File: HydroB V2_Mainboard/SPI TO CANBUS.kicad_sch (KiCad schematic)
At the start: 14 parts, among them J4 Conn_01x02_Pin, U3 MCP2515-xSO, U4 SN65HVD230, Y1 8Mhz

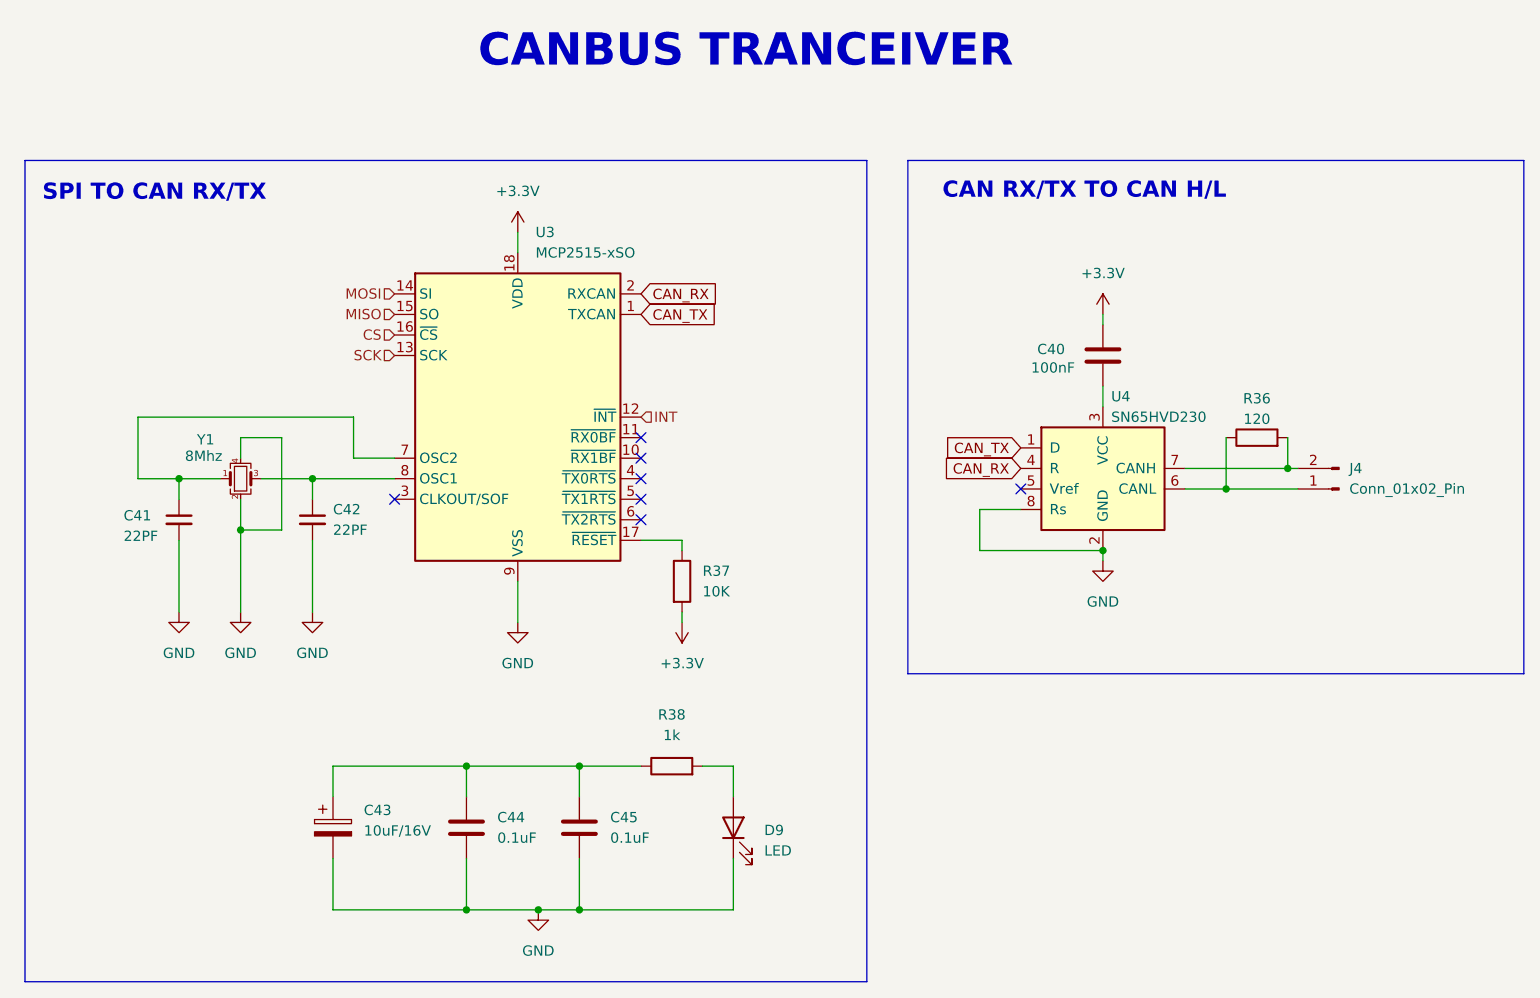
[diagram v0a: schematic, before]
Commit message: Update LCD schematic
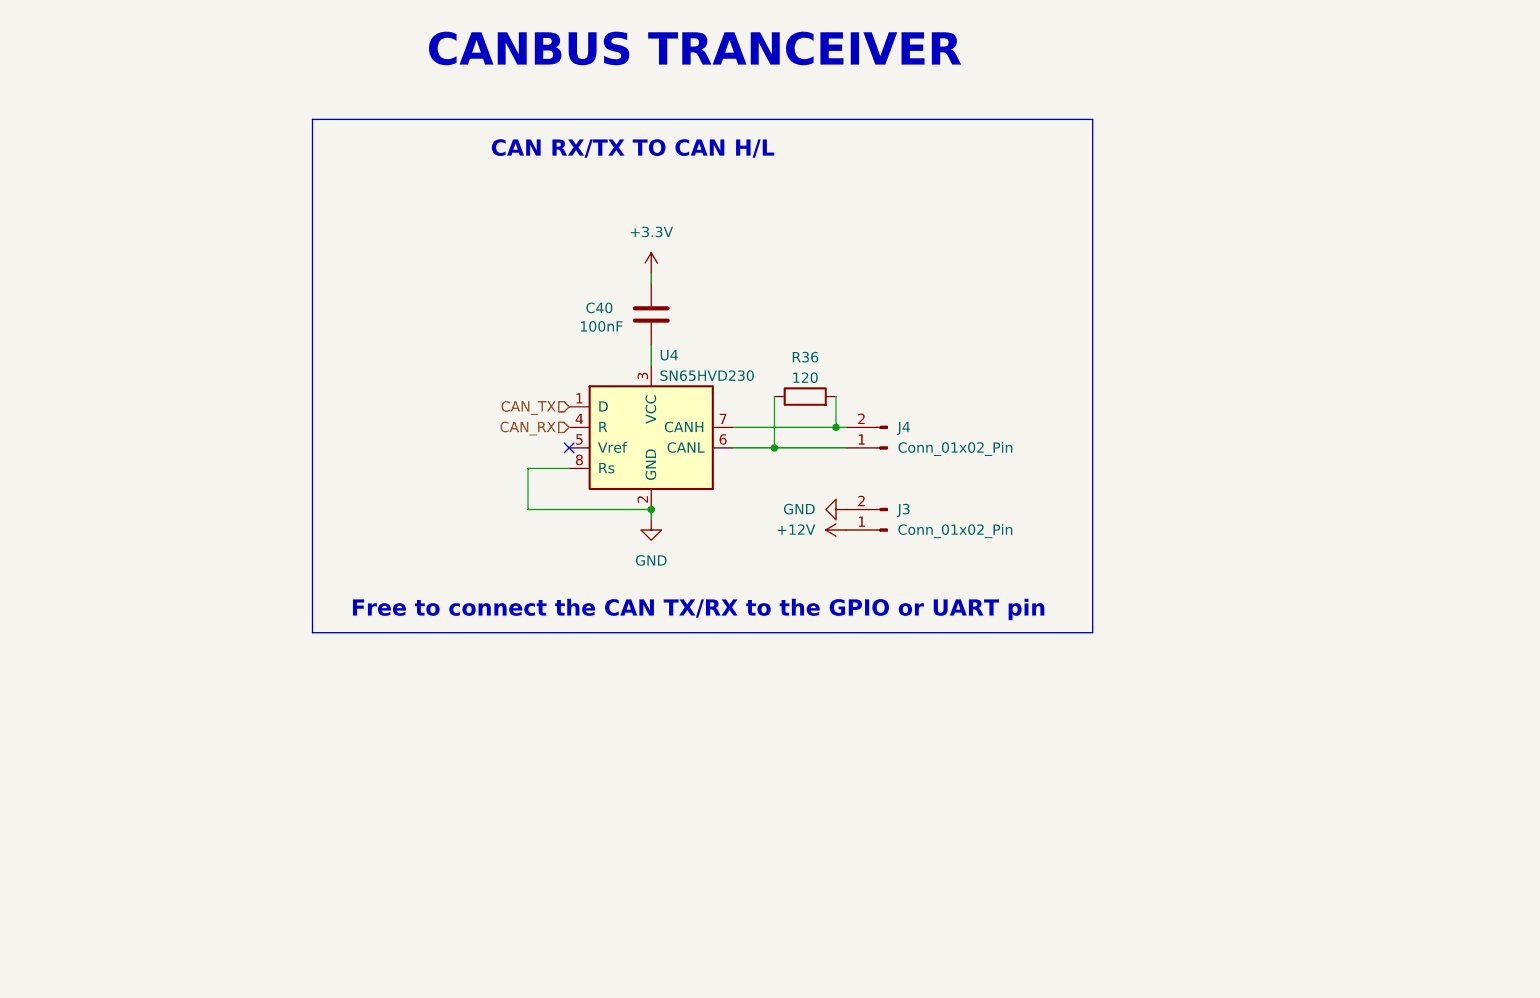
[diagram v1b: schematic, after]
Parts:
- removed C41, C42: 22PF, Capacitor_SMD:C_0603_1608Metric, symbol Device:C_Small
- removed C43: 10uF/16V, Capacitor_Tantalum_SMD:CP_EIA-7343-43_Kemet-X_Pad2.25x2.55mm_HandSolder, symbol Device:C_Polarized
- removed C44, C45: 0.1uF, Capacitor_SMD:C_0603_1608Metric, symbol Device:C
- removed D9: LED, LED_SMD:LED_0805_2012Metric, symbol Device:LED
- removed R37: 10K, Resistor_SMD:R_0603_1608Metric, symbol Device:R
- removed R38: 1k, Resistor_SMD:R_0603_1608Metric, symbol Device:R
- removed U3: MCP2515-xSO, Package_SO:SOIC-18W_7.5x11.6mm_P1.27mm, symbol Interface_CAN_LIN:MCP2515-xSO
- removed Y1: 8Mhz, Crystal:Crystal_SMD_3225-4Pin_3.2x2.5mm, symbol Device:Crystal_GND24_Small
- added J3: Conn_01x02_Pin, symbol Connector:Conn_01x02_Pin
- J4: footprint Connector_Phoenix_MC:PhoenixContact_MCV_1,5_2-G-3.5_1x02_P3.50mm_Vertical -> (none)
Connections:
- net GND: now also J3.2 (Pin_2)
- new net +12V: J3.1 (Pin_1)
- no-connect marks 7 -> 1
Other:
- note added: "Free to connect the CAN TX/RX to the GPIO or UART pin"
- note removed: "SPI TO CAN RX/TX"
- moved on the sheet: C40, R36, U4

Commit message: Schematic mainboard update
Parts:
- added R6: 10k, Resistor_SMD:R_0603_1608Metric, symbol Device:R
- J3, J4: footprint (none) -> Connector_JST:JST_XH_B2B-XH-A_1x02_P2.50mm_Vertical
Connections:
- net GND: now also R6.1; no longer U4.8 (Rs)
- new net: R6.2, U4.8 (Rs)
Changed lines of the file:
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@@
 	)
 	(junction
-		(at 133.35 106.68)
+		(at 133.35 110.49)
 		(diameter 0)
 		(color 0 0 0 0)
@@
 	(wire
 		(pts
-			(xy 118.11 101.6) (xy 118.11 106.68)
+			(xy 118.11 101.6) (xy 118.11 102.87)
 		)
 		(stroke
@@
 	(wire
 		(pts
-			(xy 133.35 107.95) (xy 133.35 106.68)
+			(xy 133.35 111.76) (xy 133.35 110.49)
 		)
 		(stroke
@@
 	(wire
 		(pts
-			(xy 118.11 106.68) (xy 133.35 106.68)
+			(xy 118.11 110.49) (xy 133.35 110.49)
 		)
 		(stroke
@@
 		(pts
 			(xy 156.21 96.52) (xy 157.48 96.52)
+		)
+		(stroke
+			(width 0)
+			(type default)
+		)
+	)
+	(wire
+		(pts
+			(xy 133.35 110.49) (xy 133.35 106.68)
 		)
 		(stroke
@@
 			)
 		)
-		(property "Footprint" ""
+		(property "Footprint" "Connector_JST:JST_XH_B2B-XH-A_1x02_P2.50mm_Vertical"
 			(at 162.56 99.06 0)
 			(effects
@@
 	(symbol
 		(lib_id "power:GND")
-		(at 133.35 107.95 0)
+		(at 133.35 111.76 0)
 		(unit 1)
 		(exclude_from_sim no)
@@
 		(fields_autoplaced yes)
 		(property "Reference" "#PWR056"
-			(at 133.35 114.3 0)
+			(at 133.35 118.11 0)
 			(effects
 				(font
@@
 		)
 		(property "Value" "GND"
-			(at 133.35 113.03 0)
+			(at 133.35 116.84 0)
 			(effects
 				(font
@@
 		)
 		(property "Footprint" ""
-			(at 133.35 107.95 0)
+			(at 133.35 111.76 0)
 			(effects
 				(font
@@
 		)
 		(property "Datasheet" ""
-			(at 133.35 107.95 0)
+			(at 133.35 111.76 0)
 			(effects
 				(font
@@
 		)
 		(property "Description" "Power symbol creates a global label with name \"GND\" , ground"
-			(at 133.35 107.95 0)
+			(at 133.35 111.76 0)
 			(effects
 				(font
@@
 			)
 		)
-		(property "Footprint" ""
+		(property "Footprint" "Connector_JST:JST_XH_B2B-XH-A_1x02_P2.50mm_Vertical"
 			(at 162.56 109.22 0)
 			(effects
@@
 					(unit 1)
 				)
+			)
+		)
+	)
+	(symbol
+		(lib_id "Device:R")
+		(at 118.11 106.68 180)
+		(unit 1)
+		(exclude_from_sim no)
+		(in_bom yes)
+		(on_board yes)
+		(dnp no)
+		(property "Reference" "R6"
+			(at 114.3 105.664 0)
+			(effects
+				(font
+					(size 1.27 1.27)
+				)
+			)
+		)
+		(property "Value" "10k"
+			(at 114.3 108.204 0)
+			(effects
+				(font
+					(size 1.27 1.27)
+				)
+			)
+		)
+		(property "Footprint" "Resistor_SMD:R_0603_1608Metric"
+			(at 119.888 106.68 90)
+			(effects
+				(font
+					(size 1.27 1.27)
+				)
+				(hide yes)
+			)
+		)
+		(property "Datasheet" "~"
+			(at 118.11 106.68 0)
+			(effects
+				(font
+					(size 1.27 1.27)
+				)
+				(hide yes)
+			)
+		)
+		(property "Description" "Resistor"
+			(at 118.11 106.68 0)
+			(effects
+				(font
+					(size 1.27 1.27)
+				)
+				(hide yes)
+			)
+		)
+		(pin "1"
+		)
+		(pin "2"
+		)
+		(instances
+			(project "LCD High Revolution"
+				(path "/7eaed49e-949c-4b32-bb59-42041e199453/cb3a589e-3872-4cde-9770-3d39d4934022/7b0d8688-cf5a-48d2-a8a1-82d926c7adcf"
+					(reference "R6")
+					(unit 1)
+				)
